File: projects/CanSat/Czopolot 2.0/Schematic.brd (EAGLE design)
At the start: 43 x 31.8 mm, 88 parts

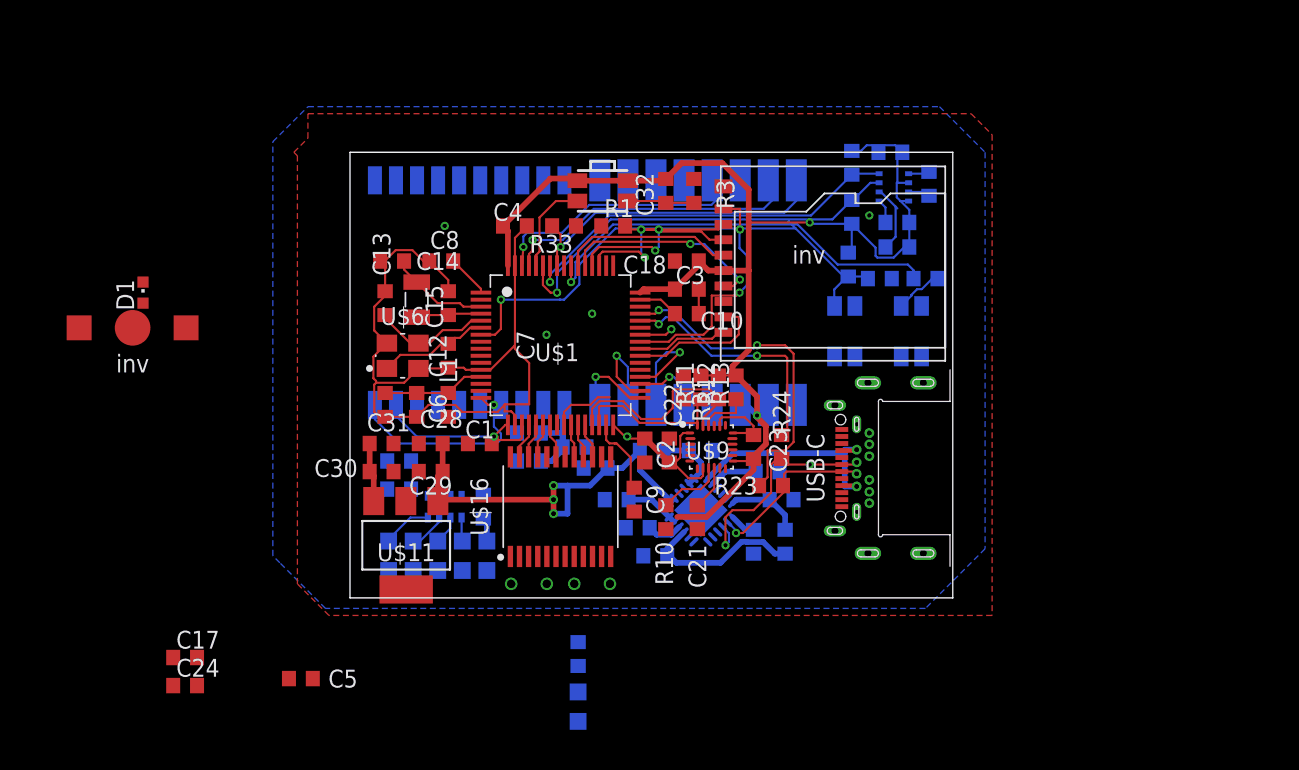
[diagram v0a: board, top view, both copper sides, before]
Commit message: Revert "Motor driver added"
This reverts commit 75eb9b0d133b9a877f65968a5a8719895b875b89.
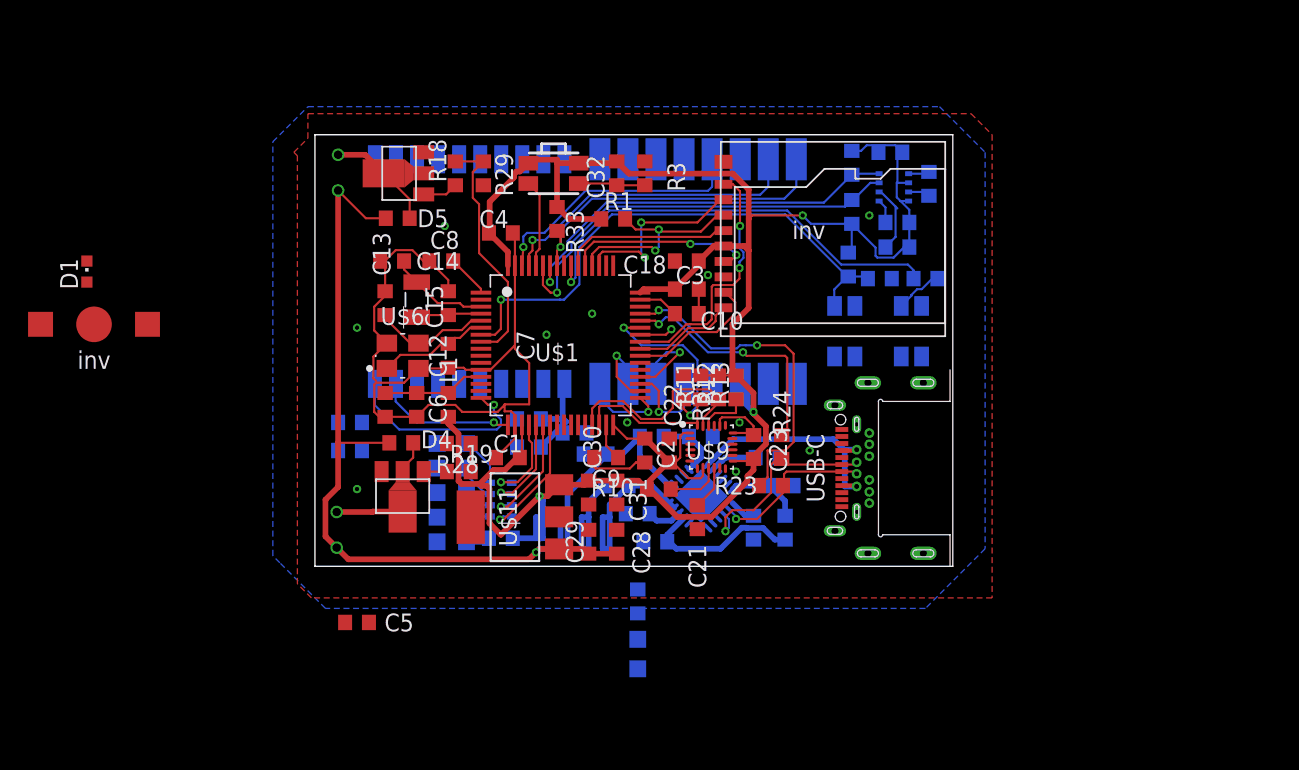
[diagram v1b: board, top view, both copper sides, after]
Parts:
- removed C17: 100n, Unified:C0603
- removed C24: 10uF pol, Unified:C0603
- removed U$16: TB6612FNG, SobieskiSat2:SOP65P760X140-24N
- removed U$17, U$18: MOTOR, Unified:INV_MOTOR
- added D4, D5: ZENER, Unified:R0603
- added R18, R19, R28, R29: ?10k, Unified:R0603
- added U$12, U$13: MOTOR, Unified:INV_MOTOR
- added U$14, U$15: NMOSFET, SobieskiSat2:INV_SOT-89
- moved C31 17.1 mm to (16.8, 5.25), turned to 270 degrees
- moved C28 15.0 mm to (16.8, 1.75), turned to 90 degrees
- moved C30 14.8 mm to (14.8, 5.25), turned to 270 degrees
- moved C29 12.3 mm to (14.8, 1.75), turned to 90 degrees
- moved D9 9.18 mm to (5.00, 8.75), turned to 270 degrees
- moved U$11 8.00 mm to (9.50, 3.50), turned to 90 degrees
- moved D8 6.83 mm to (5.00, 7.00), turned to 270 degrees
- moved D2 5.67 mm to (18.2, -6.25)
- moved R5 5.67 mm to (18.2, -2.50)
- moved C5 5.66 mm to (-1.75, -4.00)
- moved D7 4.61 mm to (5.00, 5.25), turned to 270 degrees
- moved D61 4.45 mm to (-2.25, 8.25)
- moved R63 4.45 mm to (-2.25, 10.2)
- moved D1 4.27 mm to (-21.0, 21.0)
- moved RN1 4.03 mm to (8.50, 4.75), turned to 90 degrees
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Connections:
- removed net MOT_AIN1: U$1.22, U$16.21
- removed net MOT_AIN2: U$1.21, U$16.22
- removed net MOT_BIN1: U$1.26, U$16.17
- removed net MOT_BIN2: U$1.27, U$16.16
- removed net MOT_PWMA: U$1.20, U$16.23
- removed net MOT_PWMB: U$1.28, U$16.15
- removed net MOT_STBY: U$1.23, U$16.19
- removed net N$29: U$16.11, U$16.12, U$18.P$2
- removed net N$30: U$16.7, U$16.8, U$18.P$1
- removed net N$31: U$16.5, U$16.6, U$17.P$1
- removed net N$32: U$16.1, U$16.2, U$17.P$2
- removed net N$34: U$1.24
- new net IN_MOT1: R19.2, R28.2
- new net IN_MOT2: R18.2, R29.2, U$1.8
- new net N$1: RN1.8, U$1.23
- new net N$2: RN1.6, U$1.21
- new net N$26: R19.1, U$14.1
- new net N$3: RN1.7, U$1.22
- new net N$41: D5.1, U$13.P$1, U$15.2, U$15.2@1
- new net N$42: D4.1, U$12.P$1, U$14.2, U$14.2@1
- new net N$5: R18.1, U$15.1
- new net N$50: RN1.5, U$1.20
- net GND: now also R28.1, R29.1, U$14.3, U$15.3; no longer C17.2, C24.2, U$16.10, U$16.18, U$16.3, U$16.4, U$16.9
- net MPU_INT: no longer U$1.25
- net VCC: no longer C17.1, C24.1, U$16.20
- net VSYS: now also D4.2, D5.2, U$12.P$2, U$13.P$2; no longer U$16.13, U$16.14, U$16.24
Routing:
- net VSYS: track 29.8 -> 75.7 mm, vias 3 -> 1
- net VCC: track 116.1 -> 161.7 mm, vias 2 -> 3
- net IN_MOT2: track 0.00 -> 17.7 mm
- net GND: track 68.0 -> 82.8 mm, vias 6 -> 11
- net N$37: track 0.00 -> 12.9 mm, vias 0 -> 2
- net N$1: track 0.00 -> 9.31 mm, vias 0 -> 1
- net BAT: track 3.91 -> 12.2 mm
- net N$3: track 0.00 -> 8.17 mm, vias 0 -> 1
- net N$41: track 0.00 -> 7.76 mm
- net N$2: track 0.00 -> 7.16 mm, vias 0 -> 1
- net N$42: track 0.00 -> 7.07 mm
- net N$50: track 0.00 -> 6.58 mm, vias 0 -> 1
- net MPU_INT: track 4.60 -> 0.00 mm
- net N$9: track 5.60 -> 2.68 mm
- net MOT_PWMA: track 2.56 -> 0.00 mm
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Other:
- board size 43 x 31.8 mm -> 45.5 x 30.8 mm

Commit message: Version 0.2
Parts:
- removed D4, D5: ZENER, Unified:R0603
- removed R28, R29: ?10k, Unified:R0603
- removed U$12, U$13: MOTOR, Unified:INV_MOTOR
- added C17, C25, C27, C33: 100n, Unified:C0603
- added C24, C26: 10u, Unified:C0603
- added MOTL, MOTR: MOTOR, Unified:INV_MOTOR
- BTN_RST, BTN_USR: value PUSH-SWITCH -> PUSH-SWITCHTACT_3X6; device SobieskiSat2:SWITCH_SMD -> SobieskiSat2:TACTHALF_SMD
- R18, R19: value ?10k -> 100k
- U$14, U$15: value NMOSFET -> DRV8838; device SobieskiSat2:INV_SOT-89 -> SobieskiSat2:SON50P200X200X80-9T90X160N
- moved U$15 21.9 mm to (4.50, 6.25), turned to 0 degrees
- moved U$14 20.8 mm to (2.75, 26.8), turned to 0 degrees
- moved C5 11.2 mm to (9.25, -2.00)
- moved R1 8.38 mm to (24.5, 27.2), turned to 270 degrees
- moved R30 8.07 mm to (6.25, -5.75)
- moved C1 7.67 mm to (11.5, 15.0), turned to 270 degrees
- moved C9 7.16 mm to (14.5, 14.8), turned to 0 degrees
- moved R16 6.91 mm to (22.0, 1.25), turned to 180 degrees
- moved R4 6.49 mm to (32.5, 18.8)
- moved R2 6.37 mm to (39.0, 18.8), turned to 180 degrees
- moved D6 6.04 mm to (10.5, 6.00), turned to 90 degrees
- moved R31 5.94 mm to (23.8, 18.2), turned to 180 degrees
- moved C21 5.86 mm to (26.2, 8.00), turned to 180 degrees
- moved BTN_DFU 5.55 mm to (17.8, 28.8)
- moved D9 5.55 mm to (10.5, 8.00), turned to 90 degrees
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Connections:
- removed net IN_MOT1: R19.2, R28.2
- removed net IN_MOT2: R18.2, R29.2, U$1.8
- removed net N$4 (its old number): U$1.42
- removed net N$41: D5.1, U$13.P$1, U$15.2, U$15.2@1
- removed net N$42: D4.1, U$12.P$1, U$14.2, U$14.2@1
- removed net N$43: D6.A, RN1.1
- removed net N$44: D7.A, RN1.2
- removed net N$45: D8.A, RN1.3
- removed net N$49: D9.A, RN1.4
- removed net N$50: RN1.5, U$1.20
- new net DAC1: U$1.20
- new net DAC2: U$1.21
- new net EN_L: U$1.8, U$14.5
- new net EN_R: U$1.15, U$15.5
- new net N$29: RN1.3, U$1.23
- new net N$30: C25.2, C26.2, U$14.8
- new net N$31: R18.1, U$14.7
- new net N$32: RN1.2, U$1.24
- new net N$33: RN1.1, U$1.25
- new net N$34: MOTR.P$2, U$15.2
- new net N$36: MOTR.P$1, U$15.3
- new net N$37: D7.A, RN1.7
- new net N$38: D6.A, RN1.8
- new net N$39: C17.2, C24.2, U$15.8
- new net N$40: R19.1, U$15.7
- new net PH_L: U$1.9, U$14.6
- new net PH_R: U$1.14, U$15.6
- net GND: now also C17.1, C24.1, C25.1, C26.1, C27.1, C33.1, U$14.4, U$14.9, U$15.4, U$15.9, U$2.GND, U$2.SW2; no longer BTN_RST.P$4, BTN_USR.P$4, R28.1, R29.1, U$14.3, U$15.3, U$2.P$10, U$2.P$6
- net N$1: now also D9.A, RN1.5; no longer RN1.8, U$1.23
- net N$16: no longer BTN_USR.P$3
- net N$2: now also D8.A; no longer U$1.21
- net N$26: now also MOTL.P$1, U$14.3; no longer R19.1, U$14.1
- net N$3: now also RN1.4; no longer RN1.7
- net N$5: now also MOTL.P$2, U$14.2; no longer R18.1, U$15.1
- net N$7: no longer BTN_RST.P$3
- net SD_CLK: now also U$2.CLK; no longer U$2.P$5
- net SD_CMD: now also U$2.CMD; no longer U$2.P$3
- net SD_D0: now also U$2.D0; no longer U$2.P$7
- net SD_D1: now also U$2.D1; no longer U$2.P$8
- net SD_D2: now also U$2.D2; no longer U$2.P$1
- net SD_D3: now also U$2.D3; no longer U$2.P$2
- net SD_SW: now also U$2.SW1; no longer U$2.P$9
- net VCC: now also R18.2, R19.2, U$2.VCC; no longer U$2.P$4
- net VSYS: now also C27.2, C33.2, U$14.1, U$15.1; no longer D4.2, D5.2, U$12.P$2, U$13.P$2
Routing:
- net VCC: track 161.7 -> 13.8 mm, vias 3 -> 0
- net GND: track 82.8 -> 0.00 mm, vias 11 -> 0
- net VSYS: track 75.7 -> 24.1 mm, vias 1 -> 0
- net N$35: track 23.7 -> 0.00 mm, vias 2 -> 0
- net IN_MOT2: track 17.7 -> 0.00 mm
- net N$25: track 17.4 -> 0.00 mm, vias 2 -> 0
- net N$15: track 31.4 -> 15.9 mm
- net SD_CMD: track 12.0 -> 27.1 mm, vias 0 -> 2
- net N$7: track 38.3 -> 23.5 mm
- net GPS_RX: track 14.1 -> 0.00 mm, vias 1 -> 0
- net SD_CLK: track 13.6 -> 26.6 mm, vias 2 -> 0
- net N$4: track 12.9 -> 0.00 mm, vias 2 -> 0
- net SD_D1: track 7.38 -> 20.1 mm, vias 0 -> 2
- net N$22: track 11.8 -> 0.00 mm
- net N$10: track 11.3 -> 0.00 mm
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- removed copper zone on layer 1, net GND
- removed copper zone on layer 16, net GND
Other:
- board size 45.5 x 30.8 mm -> 40.2 x 30.8 mm
- board text added: "^ Battery and switch holes or pads"

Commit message: Version 0.3
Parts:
- removed R12: 10k, Unified:R0603
- added BAT_PACK: (no value), SobieskiSat2:2X1_2.54
- added U$12: 50R, SobieskiSat2:CON_U.FL
- L2: device Unified:R0603 -> Unified:R1206
- MOTL, MOTR: device Unified:INV_MOTOR -> Unified:2X1_2.54
- R11: value 10k -> 100k
- moved R16 38.6 mm to (60.5, -1.50)
- moved R17 38.6 mm to (58.8, -1.50)
- moved R15 36.6 mm to (54.8, 0.75), turned to 0 degrees
- moved R2 36.1 mm to (4.00, 27.8), turned to 90 degrees
- moved C16 35.1 mm to (51.5, 0.75)
- moved C11 34.9 mm to (2.00, 27.8), turned to 270 degrees
- moved C35 34.4 mm to (49.2, 2.50), turned to 270 degrees
- moved R14 33.8 mm to (60.2, 5.25), turned to 180 degrees
- moved C37 31.8 mm to (60.2, 3.25), turned to 180 degrees
- moved D61 31.3 mm to (16.0, 37.0), turned to 90 degrees
- moved U$10 30.0 mm to (52.8, 4.75), turned to 0 degrees
- moved L2 28.4 mm to (47.2, 4.75), turned to 90 degrees
- moved BTN_RST 27.6 mm to (10.2, 26.5)
- moved BTN_USR 26.7 mm to (10.2, 29.0), turned to 180 degrees
- moved R63 26.5 mm to (16.0, 33.5), turned to 90 degrees
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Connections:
- net N$10 renamed DFU
- net N$7 renamed NRST
- removed net BMP_SCL: R6.1, U$1.58, U$8.4
- removed net BMP_SDA: R7.1, U$1.59, U$8.3
- removed net DAC1: U$1.20
- removed net DAC2: U$1.21
- removed net MPU_SCL: R12.1, U$1.29, U$9.23
- removed net MPU_SDA: R11.1, U$1.30, U$9.24
- removed net N$19: B6.P$1, U$3.P$4
- removed net N$29: RN1.3, U$1.23
- removed net N$3: RN1.4, U$1.22
- removed net N$32: RN1.2, U$1.24
- removed net N$33: RN1.1, U$1.25
- removed net N$4 (its old number): R31.2, U$1.43
- new net N$7: R11.2, U$1.28
- new net SCL: R7.2, U$1.29, U$8.4, U$9.23
- new net SDA: R6.2, U$1.30, U$8.3, U$9.24
- net BAT: now also BAT_PACK.P$1
- net GND: now also BAT_PACK.P$2, R11.1, U$12.GND, U$12.GND@1
- net GPS_RX: now also U$1.42; no longer U$1.16
- net GPS_TX: now also R31.2, U$1.43; no longer U$1.17
- net LR_ANT: now also U$12.SIG
- net LR_MISO: now also U$1.22; no longer U$1.35
- net LR_MOSI: now also U$1.23; no longer U$1.36
- net LR_NSS: now also U$1.20; no longer U$1.33
- net LR_SCK: now also U$1.21; no longer U$1.34
- net VBACKUP: now also B6.P$1, U$3.P$4
- net VCC: now also R6.1, R7.1; no longer R11.2, R12.2, R6.2, R7.2
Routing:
- net VCC: track 13.8 -> 142.5 mm, vias 0 -> 4
- net GND: track 0.00 -> 122.1 mm, vias 0 -> 15
- net VSYS: track 24.1 -> 57.4 mm
- net BMP_SDA: track 27.9 -> 0.00 mm, vias 1 -> 0
- net SCL: track 0.00 -> 27.1 mm, vias 0 -> 1
- net SDA: track 0.00 -> 26.6 mm, vias 0 -> 1
- net BMP_SCL: track 24.6 -> 0.00 mm, vias 1 -> 0
- net GPS_TX: track 0.00 -> 23.2 mm, vias 0 -> 1
- net GPS_RX: track 0.00 -> 16.8 mm, vias 0 -> 1
- net USB_VBUS: track 17.8 -> 2.17 mm
- net LR_NSS: track 6.74 -> 20.5 mm
- net SD_D0: track 20.2 -> 33.0 mm
- net SD_D1: track 20.1 -> 32.7 mm, vias 2 -> 0
- net MPU_SCL: track 12.4 -> 0.00 mm
- net LR_BUSY: track 19.3 -> 6.95 mm
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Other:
- board size 40.2 x 30.8 mm -> 43 x 30.8 mm

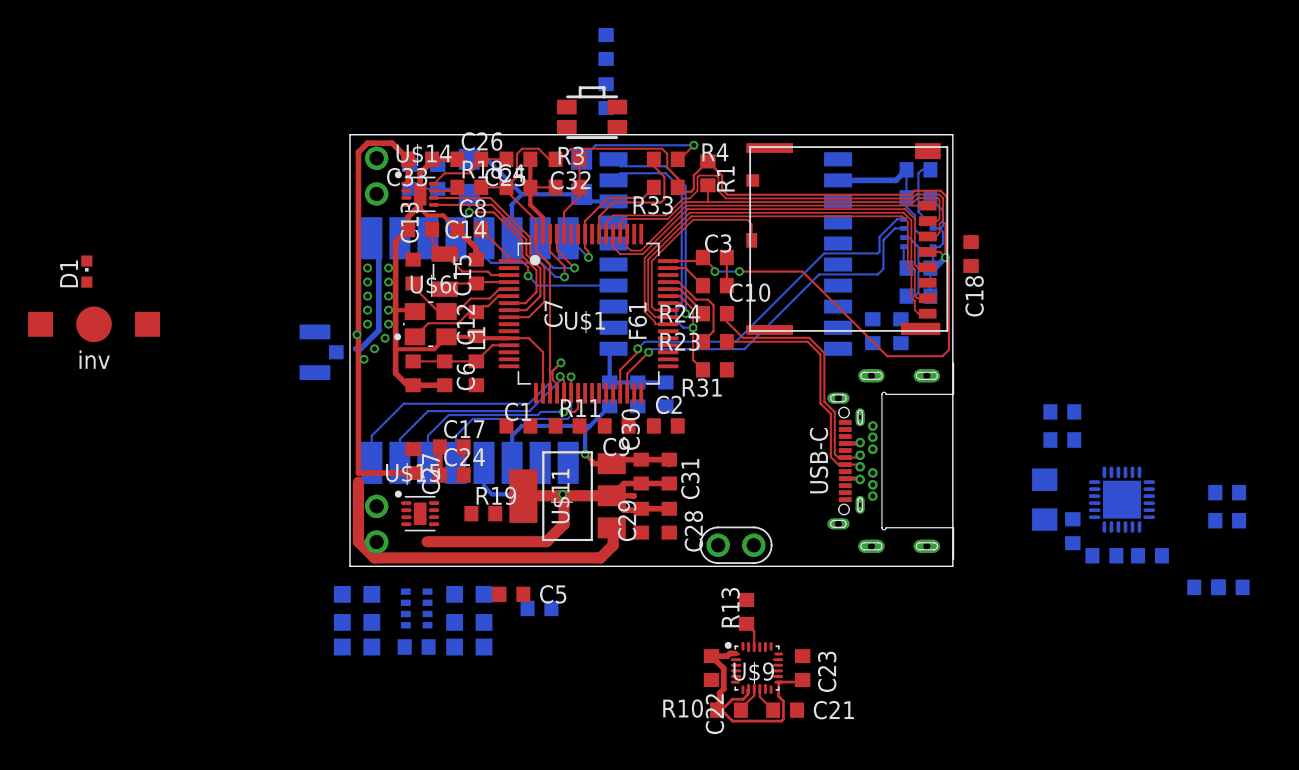
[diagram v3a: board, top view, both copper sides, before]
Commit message: Motor driver changed
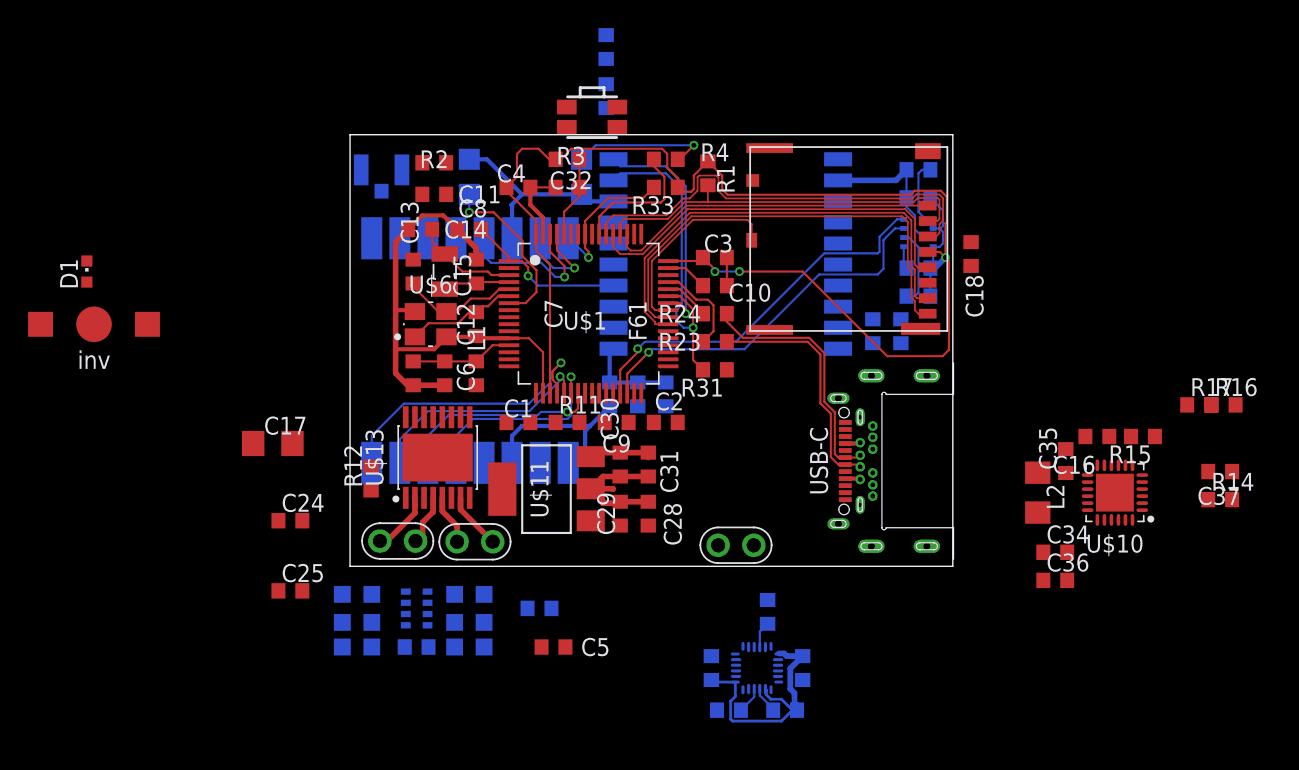
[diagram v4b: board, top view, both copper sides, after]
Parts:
- removed C26: 10u, Unified:C0603
- removed C27, C33: 100n, Unified:C0603
- removed R18, R19: 100k, Unified:R0603
- removed U$14, U$15: DRV8838, SobieskiSat2:SON50P200X200X80-9T90X160N
- added R12: 10k, Unified:R0603
- added U$13: DRV8833SOP, SobieskiSat2:SOP65P640X120-17T340X500N
- C17: value 100n -> 10u_pol; device Unified:C0603 -> Unified:C1206
- C24: value 10u -> 100n
- C25: value 100n -> 2.2u
- moved C25 34.8 mm to (-6.50, -1.75), turned to 0 degrees
- moved MOTL 26.0 mm to (1.15, 1.80), flipped to the top, turned to 180 degrees
- moved U$12 13.8 mm to (0.00, 28.2), turned to 270 degrees
- moved R16 13.0 mm to (60.0, 11.5), flipped to the top, turned to 0 degrees
- moved R17 13.0 mm to (58.2, 11.5), flipped to the top, turned to 0 degrees
- moved C17 12.8 mm to (-7.75, 8.75)
- moved C36 12.0 mm to (48.0, -1.00), flipped to the top, turned to 0 degrees
- moved C24 12.0 mm to (-6.50, 3.25)
- moved C16 8.51 mm to (51.0, 9.25), flipped to the top, turned to 180 degrees
- moved R15 8.51 mm to (54.2, 9.25), flipped to the top, turned to 180 degrees
- moved C34 8.02 mm to (48.0, 1.00), flipped to the top, turned to 0 degrees
- moved MOTR 7.11 mm to (6.65, 1.75), flipped to the top, turned to 0 degrees
- moved C22 6.50 mm to (30.0, -7.25), flipped to the bottom
- moved C23 6.50 mm to (23.5, -7.25), flipped to the bottom
- moved C35 5.02 mm to (48.8, 7.50), flipped to the top, turned to 90 degrees
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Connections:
- removed net EN_L: U$1.8, U$14.5
- removed net EN_R: U$1.15, U$15.5
- removed net N$34: MOTR.P$2, U$15.2
- removed net N$36: MOTR.P$1, U$15.3
- removed net N$39: C17.2, C24.2, U$15.8
- removed net N$40: R19.1, U$15.7
- removed net PH_L: U$1.9, U$14.6
- removed net PH_R: U$1.14, U$15.6
- new net AIN1: U$13.16
- new net AIN2: U$13.15
- new net BIN1: U$13.9
- new net BIN2: U$13.10
- new net N$10: MOTL.P$2, U$13.2
- new net N$15: MOTR.P$1, U$13.5
- new net N$19: C17.1, C24.1, U$13.11
- new net N$29: U$13.3
- new net N$3: MOTR.P$2, U$13.7
- net GND: now also U$13.13, U$13.17; no longer C17.1, C24.1, C26.1, C27.1, C33.1, U$14.4, U$14.9, U$15.4, U$15.9
- net N$26: now also C25.2, U$13.14; no longer MOTL.P$1, U$14.3
- net N$30: now also U$13.6; no longer C25.2, C26.2, U$14.8
- net N$31: now also R12.1, U$13.1; no longer R18.1, U$14.7
- net N$5: now also MOTL.P$1, U$13.4; no longer MOTL.P$2, U$14.2
- net VCC: now also R12.2; no longer R18.2, R19.2
- net VSYS: now also C17.2, C24.2, U$13.12; no longer C27.2, C33.2, U$14.1, U$15.1
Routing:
- net VSYS: track 57.4 -> 0.00 mm
- net GND: track 122.1 -> 84.0 mm, vias 15 -> 0
- net PH_L: track 16.0 -> 0.00 mm
- net EN_L: track 14.7 -> 0.00 mm
- net LR_ANT: track 8.96 -> 0.71 mm
- net N$30: track 5.98 -> 0.00 mm
- net N$10: track 0.00 -> 4.40 mm
- net NRST: track 16.7 -> 12.5 mm
- net N$3: track 0.00 -> 4.08 mm
- net VCC: track 142.5 -> 138.4 mm, vias 4 -> 3
- net N$5: track 0.00 -> 3.60 mm
- net N$15: track 0.00 -> 3.57 mm
- net N$39: track 2.38 -> 0.00 mm
- net N$31: track 1.77 -> 0.00 mm
